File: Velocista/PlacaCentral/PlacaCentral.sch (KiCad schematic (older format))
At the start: 39 parts, among them J1 Conn_01x03, J10 Conn_01x08, J11 Conn_01x02, J12 Conn_01x02, J13 Conn_01x03, J14 Conn_01x08, J15 Conn_01x02, J16 Conn_01x02, J2 Conn_01x03, J3 Conn_01x03, J4 Conn_01x03, J5 Conn_01x06, J6 Conn_01x06, J7 Conn_01x03, J8 Conn_01x03, J9 Conn_01x03, SW1 SW_Push, SW2 SW_Push, SW3 SW_DPDT_x2, U1 PCF8574, U2 DC-DC_BuckModule

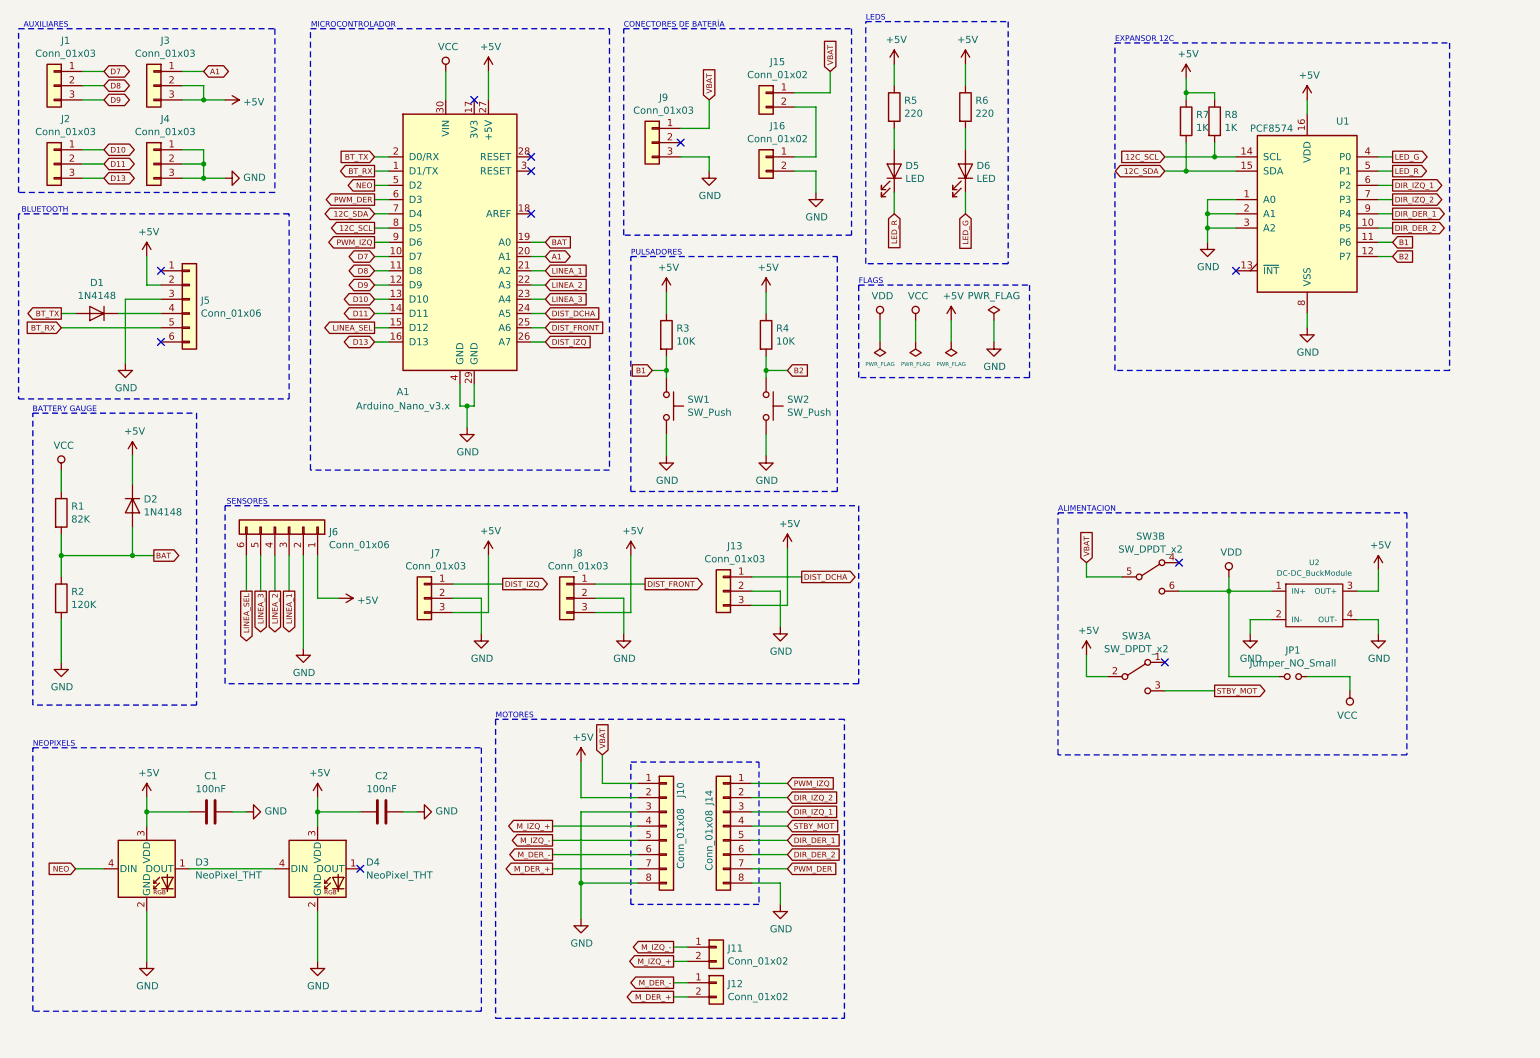
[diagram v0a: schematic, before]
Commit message: Empezado el diseño de la placa principal
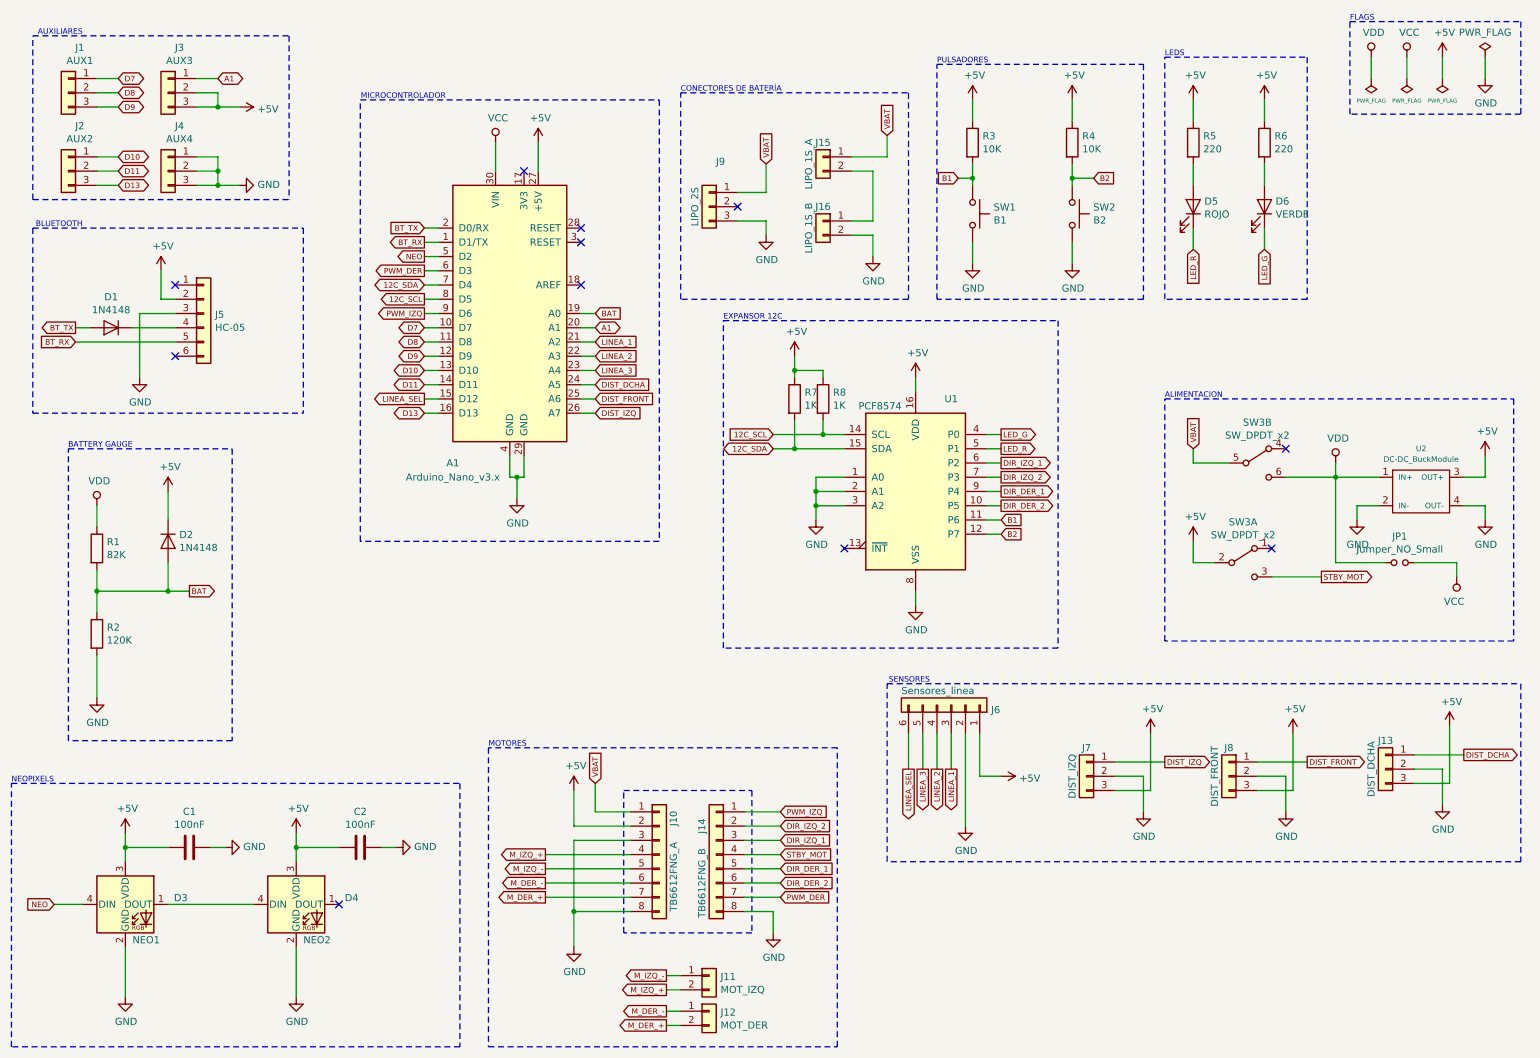
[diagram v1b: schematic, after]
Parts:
- C1, C2: footprint (none) -> Capacitor_SMD:C_0805_2012Metric_Pad1.15x1.40mm_HandSolder
- D3: value NeoPixel_THT -> NEO1; footprint (none) -> LED_THT:LED_D5.0mm-4_RGB
- D4: value NeoPixel_THT -> NEO2; footprint (none) -> LED_THT:LED_D5.0mm-4_RGB
- D5: value LED -> ROJO; footprint (none) -> LED_THT:LED_D3.0mm
- D6: value LED -> VERDE; footprint (none) -> LED_THT:LED_D3.0mm
- J1: value Conn_01x03 -> AUX1; footprint (none) -> Connector_PinHeader_2.54mm:PinHeader_1x03_P2.54mm_Vertical
- J10: value Conn_01x08 -> TB6612FNG_A; footprint (none) -> Connector_PinHeader_2.54mm:PinHeader_1x08_P2.54mm_Vertical
- J11: value Conn_01x02 -> MOT_IZQ; footprint (none) -> Connector_PinHeader_2.54mm:PinHeader_1x02_P2.54mm_Vertical
- J12: value Conn_01x02 -> MOT_DER; footprint (none) -> Connector_PinHeader_2.54mm:PinHeader_1x02_P2.54mm_Vertical
- J13: value Conn_01x03 -> DIST_DCHA; footprint (none) -> Connector_PinHeader_2.54mm:PinHeader_1x03_P2.54mm_Vertical
- J14: value Conn_01x08 -> TB6612FNG_B; footprint (none) -> Connector_PinHeader_2.54mm:PinHeader_1x08_P2.54mm_Vertical
- J15: value Conn_01x02 -> LIPO_1S_A; footprint (none) -> Connector_JST:JST_PH_B2B-PH-K_1x02_P2.00mm_Vertical
- J16: value Conn_01x02 -> LIPO_1S_B; footprint (none) -> Connector_JST:JST_PH_B2B-PH-K_1x02_P2.00mm_Vertical
- J2: value Conn_01x03 -> AUX2; footprint (none) -> Connector_PinHeader_2.54mm:PinHeader_1x03_P2.54mm_Vertical
- J3: value Conn_01x03 -> AUX3; footprint (none) -> Connector_PinHeader_2.54mm:PinHeader_1x03_P2.54mm_Vertical
- J4: value Conn_01x03 -> AUX4; footprint (none) -> Connector_PinHeader_2.54mm:PinHeader_1x03_P2.54mm_Vertical
- J5: value Conn_01x06 -> HC-05; footprint (none) -> Connector_PinHeader_2.54mm:PinHeader_1x06_P2.54mm_Vertical
- J6: value Conn_01x06 -> Sensores_linea; footprint (none) -> Connector_PinHeader_2.54mm:PinHeader_1x06_P2.54mm_Vertical
- J7: value Conn_01x03 -> DIST_IZQ; footprint (none) -> Connector_PinHeader_2.54mm:PinHeader_1x03_P2.54mm_Vertical
- J8: value Conn_01x03 -> DIST_FRONT; footprint (none) -> Connector_PinHeader_2.54mm:PinHeader_1x03_P2.54mm_Vertical
- J9: value Conn_01x03 -> LIPO_2S; footprint (none) -> Connector_JST:JST_XH_B03B-XH-A_1x03_P2.50mm_Vertical
- JP1: footprint (none) -> Jumper:SolderJumper-2_P1.3mm_Open_Pad1.0x1.5mm
- R1, R2, R3, R4, R5, R6, R7, R8: footprint (none) -> Resistor_SMD:R_0805_2012Metric_Pad1.15x1.40mm_HandSolder
- SW1: value SW_Push -> B1; footprint (none) -> Button_Switch_THT:SW_PUSH_6mm
- SW2: value SW_Push -> B2; footprint (none) -> Button_Switch_THT:SW_PUSH_6mm
- SW3: footprint (none) -> Button_Switch_THT:SW_CuK_JS202011CQN_DPDT_Straight
- U1: footprint (none) -> Package_DIP:DIP-16_W7.62mm_LongPads
- U2: footprint (none) -> PlacaCentral:DC-DC-MP2307
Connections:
- net VCC: no longer R1.1
- net VDD: now also R1.1
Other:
- moved on the sheet: A1, C1, C2, D1, D2, D3, D4, D5, D6, J1, J10, J11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
